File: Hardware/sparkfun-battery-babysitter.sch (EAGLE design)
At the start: 56 parts, among them U1 BQ24075, U2 BQ27441-G1

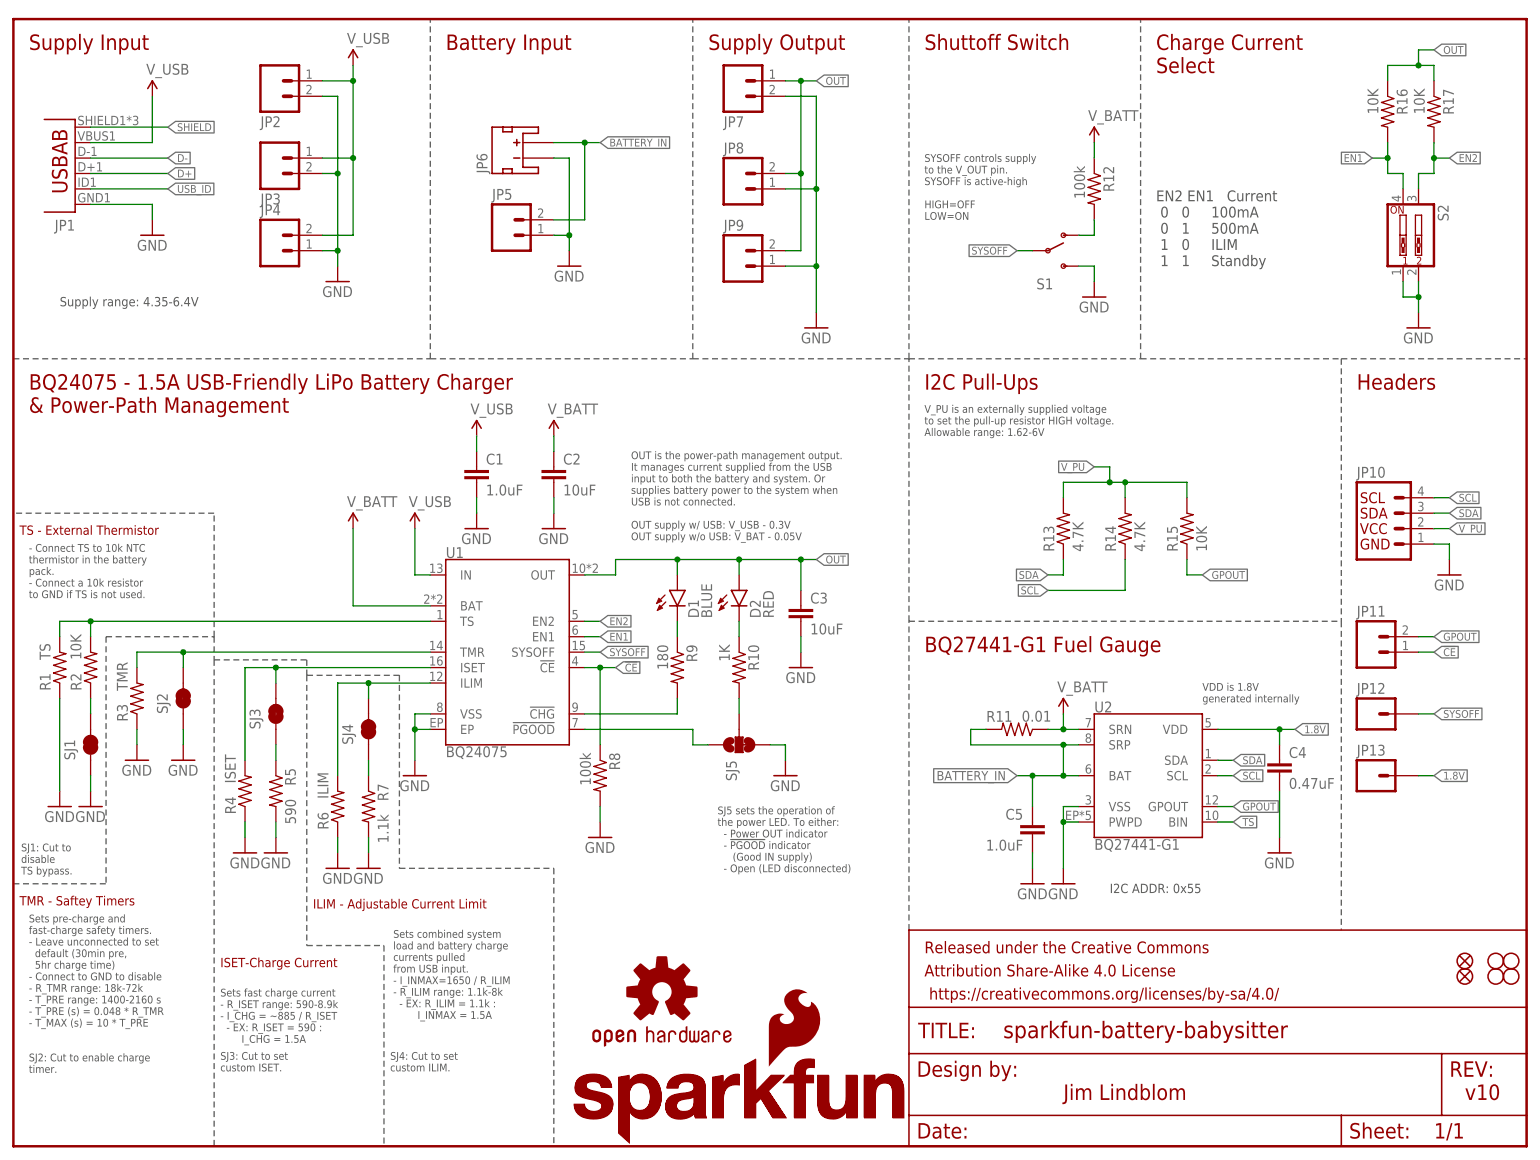
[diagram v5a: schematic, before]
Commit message: Break out D+/D-, silkscreen fixes
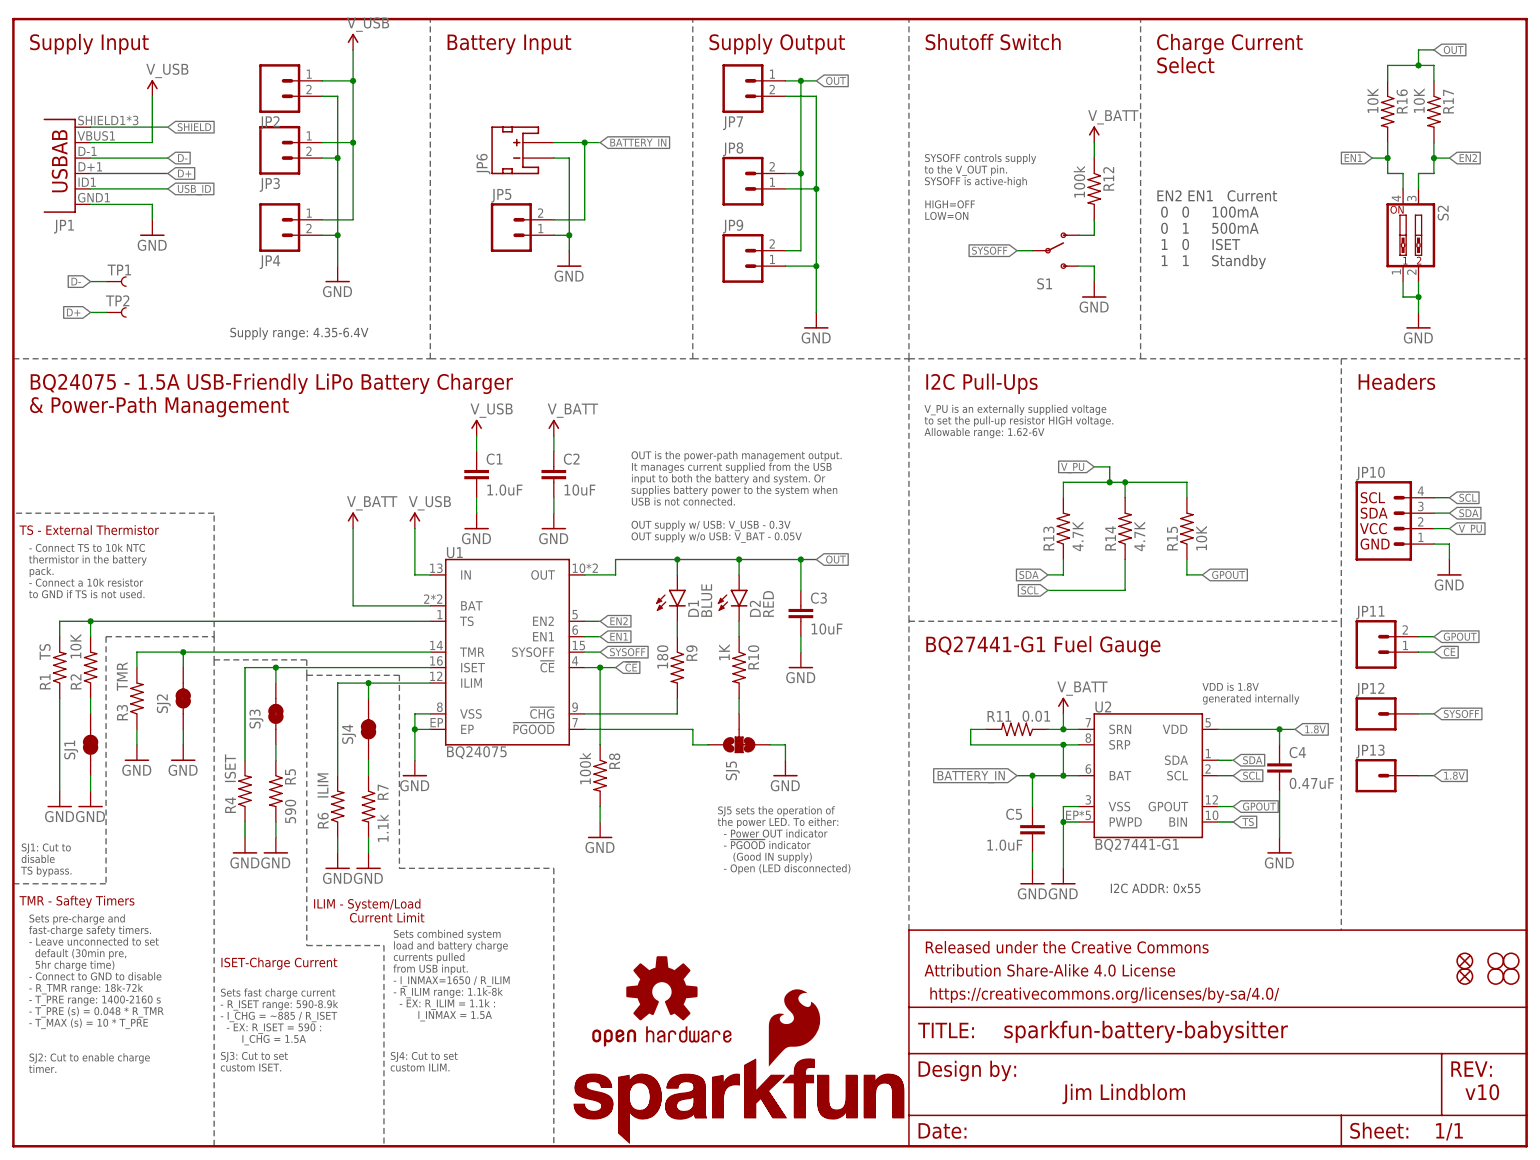
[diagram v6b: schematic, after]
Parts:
- added TP1, TP2: TEST-POINT3X4, SparkFun-Passives:TEST-POINT3X4
- JP4: device SparkFun-Connectors:M02-JST-2-PTH-NO_SILK -> SparkFun-Connectors:M021X02_NO_SILK
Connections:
- net D+: now also TP2.1
- net D-: now also TP1.1
- net GND: now also JP4.2; no longer JP4.1
- net V_USB: now also JP4.1; no longer JP4.2
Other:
- note added: "EN2 EN1 Current 0 0 100mA 0 1 500mA 1 0 ISET 1 1 Standby"
- note added: "ILIM - System/Load Current Limit"
- note added: "Shutoff Switch"
- note removed: "EN2 EN1 Current 0 0 100mA 0 1 500mA 1 0 ILIM 1 1 Standby"
- note removed: "ILIM - Adjustable Current Limit"
- note removed: "Shuttoff Switch"
- moved on the sheet: JP3, JP4
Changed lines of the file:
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@@
 <part name="R16" library="SparkFun-Resistors" deviceset="10KOHM-1/10W-1%(0603)" device="0603" value="10K"/>
 <part name="R17" library="SparkFun-Resistors" deviceset="10KOHM-1/10W-1%(0603)" device="0603" value="10K"/>
-<part name="JP2" library="SparkFun-Connectors" deviceset="M02" device="1X02_NO_SILK"/>
 <part name="R6" library="SparkFun-Resistors" deviceset="RESISTOR" device="PTH-1/6W" value="ILIM"/>
 <part name="GND8" library="SparkFun-Aesthetics" deviceset="GND" device=""/>
@@
 <part name="SJ4" library="SparkFun-Passives" deviceset="JUMPER-PAD-2-NC_BY_TRACE" device="" value=""/>
 <part name="SJ3" library="SparkFun-Passives" deviceset="JUMPER-PAD-2-NC_BY_TRACE" device="" value=""/>
-<part name="JP4" library="SparkFun-Connectors" deviceset="M02" device="-JST-2-PTH-NO_SILK"/>
+<part name="JP4" library="SparkFun-Connectors" deviceset="M02" device="1X02_NO_SILK"/>
 <part name="LOGO1" library="SparkFun-Aesthetics" deviceset="SFE_LOGO_NAME" device=".1_INCH"/>
 <part name="LOGO3" library="SparkFun-Aesthetics" deviceset="OSHW-LOGO" device="S" value="OSHW-LOGOS"/>
@@
 <part name="GND24" library="SparkFun-Aesthetics" deviceset="GND" device=""/>
 <part name="SJ5" library="SparkFun-Passives" deviceset="JUMPER-PAD-3-2OF3_NC_BY_TRACE" device="_SMALL" value=""/>
+<part name="JP2" library="SparkFun-Connectors" deviceset="M02" device="1X02_NO_SILK"/>
+<part name="TP1" library="SparkFun-Passives" deviceset="TEST-POINT" device="3X4" value=""/>
+<part name="TP2" library="SparkFun-Passives" deviceset="TEST-POINT" device="3X4" value=""/>
 </parts>
 <sheets>
@@
  0   0     100mA
  0   1     500mA
- 1   0     ILIM
+ 1   0     ISET
  1   1     Standby</text>
 <text x="34.036" y="25.908" size="1.27" layer="97" align="top-left">Sets fast charge current
@@
 <text x="71.12" y="182.88" size="2.54" layer="94" align="top-left">Battery Input</text>
 <text x="114.3" y="182.88" size="2.54" layer="94" align="top-left">Supply Output</text>
-<text x="149.86" y="182.88" size="2.54" layer="94" align="top-left">Shuttoff Switch</text>
+<text x="149.86" y="182.88" size="2.54" layer="94" align="top-left">Shutoff Switch</text>
 <text x="187.96" y="182.88" size="2.54" layer="94" align="top-left">Charge Current
 Select</text>
@@
 <wire x1="15.24" y1="83.82" x2="33.02" y2="83.82" width="0.2032" layer="97" style="shortdash"/>
 <wire x1="33.02" y1="83.82" x2="33.02" y2="80.01" width="0.2032" layer="97" style="shortdash"/>
-<text x="49.276" y="40.64" size="1.524" layer="94" align="top-left">ILIM - Adjustable Current Limit</text>
+<text x="49.276" y="40.64" size="1.524" layer="94" align="top-left">ILIM - System/Load
+          Current Limit</text>
 <text x="34.036" y="30.988" size="1.524" layer="94" align="top-left">ISET-Charge Current</text>
 <text x="1.016" y="41.148" size="1.524" layer="94" align="top-left">TMR - Saftey Timers</text>
@@
 to set the pull-up resistor HIGH voltage.
 Allowable range: 1.62-6V</text>
-<text x="7.62" y="139.7" size="1.524" layer="97" align="top-left">Supply range: 4.35-6.4V</text>
+<text x="35.56" y="134.62" size="1.524" layer="97" align="top-left">Supply range: 4.35-6.4V</text>
 <text x="195.58" y="76.2" size="1.27" layer="97" align="top-left">VDD is 1.8V
 generated internally</text>
@@
 <instance part="R16" gate="G$1" x="226.06" y="170.18" rot="R270"/>
 <instance part="R17" gate="G$1" x="233.68" y="170.18" rot="R270"/>
-<instance part="JP2" gate="G$1" x="43.18" y="175.26" rot="MR180"/>
 <instance part="R6" gate="G$1" x="53.34" y="55.88" smashed="yes" rot="R90">
 <attribute name="NAME" x="51.8414" y="52.07" size="1.778" layer="95" rot="R90"/>
@@
 <instance part="GND11" gate="1" x="76.2" y="101.6"/>
 <instance part="C1" gate="G$1" x="76.2" y="109.22"/>
-<instance part="SUPPLY2" gate="G$1" x="55.88" y="177.8"/>
+<instance part="SUPPLY2" gate="G$1" x="55.88" y="180.34"/>
 <instance part="GND7" gate="1" x="53.34" y="142.24"/>
 <instance part="STANDOFF3" gate="G$1" x="246.38" y="30.48"/>
@@
 <instance part="STANDOFF4" gate="G$1" x="246.38" y="27.94"/>
 <instance part="S1" gate="1" x="170.18" y="147.32"/>
-<instance part="JP3" gate="G$1" x="43.18" y="162.56" rot="MR180"/>
+<instance part="JP3" gate="G$1" x="43.18" y="165.1" rot="MR180"/>
 <instance part="JP7" gate="G$1" x="119.38" y="175.26" rot="MR180"/>
 <instance part="JP8" gate="G$1" x="119.38" y="157.48"/>
@@
 <instance part="SJ4" gate="G$1" x="58.42" y="68.58" rot="R90"/>
 <instance part="SJ3" gate="G$1" x="43.18" y="71.12" rot="R90"/>
-<instance part="JP4" gate="G$1" x="43.18" y="147.32"/>
+<instance part="JP4" gate="G$1" x="43.18" y="152.4" rot="MR180"/>
 <instance part="LOGO1" gate="G$1" x="90.17" y="0.508"/>
 <instance part="LOGO3" gate="G$1" x="106.68" y="25.4"/>
@@
 <instance part="GND24" gate="1" x="127" y="60.96"/>
 <instance part="SJ5" gate="G$1" x="119.38" y="66.04" rot="MR270"/>
+<instance part="JP2" gate="G$1" x="43.18" y="175.26" rot="MR180"/>
+<instance part="TP1" gate="G$1" x="15.24" y="142.24" smashed="yes">
+<attribute name="NAME" x="15.494" y="143.256" size="1.778" layer="95"/>
+<attribute name="VALUE" x="12.7" y="139.7" size="1.778" layer="96"/>
+</instance>
+<instance part="TP2" gate="G$1" x="15.24" y="137.16" smashed="yes">
+<attribute name="NAME" x="15.24" y="138.176" size="1.778" layer="95"/>
+<attribute name="VALUE" x="12.7" y="134.62" size="1.778" layer="96"/>
+</instance>
 </instances>
 <busses>
@@
 <segment>
 <pinref part="GND7" gate="1" pin="GND"/>
-<wire x1="53.34" y1="172.72" x2="53.34" y2="160.02" width="0.1524" layer="91"/>
+<wire x1="53.34" y1="162.56" x2="53.34" y2="149.86" width="0.1524" layer="91"/>
+<pinref part="JP3" gate="G$1" pin="2"/>
+<wire x1="53.34" y1="149.86" x2="53.34" y2="144.78" width="0.1524" layer="91"/>
+<wire x1="50.8" y1="162.56" x2="53.34" y2="162.56" width="0.1524" layer="91"/>
+<pinref part="JP4" gate="G$1" pin="2"/>
+<wire x1="50.8" y1="149.86" x2="53.34" y2="149.86" width="0.1524" layer="91"/>
+<junction x="53.34" y="149.86"/>
 <pinref part="JP2" gate="G$1" pin="2"/>
-<wire x1="53.34" y1="160.02" x2="53.34" y2="147.32" width="0.1524" layer="91"/>
-<wire x1="53.34" y1="147.32" x2="53.34" y2="144.78" width="0.1524" layer="91"/>
 <wire x1="50.8" y1="172.72" x2="53.34" y2="172.72" width="0.1524" layer="91"/>
-<pinref part="JP3" gate="G$1" pin="2"/>
-<wire x1="50.8" y1="160.02" x2="53.34" y2="160.02" width="0.1524" layer="91"/>
-<junction x="53.34" y="160.02"/>
-<pinref part="JP4" gate="G$1" pin="1"/>
-<wire x1="50.8" y1="147.32" x2="53.34" y2="147.32" width="0.1524" layer="91"/>
-<junction x="53.34" y="147.32"/>
+<wire x1="53.34" y1="172.72" x2="53.34" y2="162.56" width="0.1524" layer="91"/>
+<junction x="53.34" y="162.56"/>
 </segment>
 <segment>
@@
 <label x="25.4" y="160.02" size="1.27" layer="95" xref="yes"/>
 </segment>
+<segment>
+<pinref part="TP2" gate="G$1" pin="1"/>
+<wire x1="15.24" y1="137.16" x2="12.7" y2="137.16" width="0.1524" layer="91"/>
+<label x="12.7" y="137.16" size="1.27" layer="95" rot="R180" xref="yes"/>
+</segment>
 </net>
 <net name="D-" class="0">
@@
 <wire x1="12.7" y1="162.56" x2="25.4" y2="162.56" width="0.1524" layer="91"/>
 <label x="25.4" y="162.56" size="1.27" layer="95" xref="yes"/>
+</segment>
+<segment>
+<pinref part="TP1" gate="G$1" pin="1"/>
+<wire x1="15.24" y1="142.24" x2="12.7" y2="142.24" width="0.1524" layer="91"/>
+<label x="12.7" y="142.24" size="1.27" layer="95" rot="R180" xref="yes"/>
 </segment>
 </net>
@@
 <segment>
 <pinref part="SUPPLY2" gate="G$1" pin="V_USB"/>
-<wire x1="55.88" y1="162.56" x2="55.88" y2="175.26" width="0.1524" layer="91"/>
+<wire x1="55.88" y1="165.1" x2="55.88" y2="175.26" width="0.1524" layer="91"/>
 <pinref part="JP3" gate="G$1" pin="1"/>
-<wire x1="55.88" y1="175.26" x2="55.88" y2="177.8" width="0.1524" layer="91"/>
-<wire x1="50.8" y1="162.56" x2="55.88" y2="162.56" width="0.1524" layer="91"/>
+<wire x1="55.88" y1="175.26" x2="55.88" y2="180.34" width="0.1524" layer="91"/>
+<wire x1="50.8" y1="165.1" x2="55.88" y2="165.1" width="0.1524" layer="91"/>
+<wire x1="55.88" y1="152.4" x2="55.88" y2="165.1" width="0.1524" layer="91"/>
+<junction x="55.88" y="165.1"/>
+<pinref part="JP4" gate="G$1" pin="1"/>
+<wire x1="50.8" y1="152.4" x2="55.88" y2="152.4" width="0.1524" layer="91"/>
 <pinref part="JP2" gate="G$1" pin="1"/>
 <wire x1="50.8" y1="175.26" x2="55.88" y2="175.26" width="0.1524" layer="91"/>
 <junction x="55.88" y="175.26"/>
-<pinref part="JP4" gate="G$1" pin="2"/>
-<wire x1="50.8" y1="149.86" x2="55.88" y2="149.86" width="0.1524" layer="91"/>
-<wire x1="55.88" y1="149.86" x2="55.88" y2="162.56" width="0.1524" layer="91"/>
-<junction x="55.88" y="162.56"/>
 </segment>
 </net>

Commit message: Small silk fixes after run through checklist
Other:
- note added: "Battery Range: 3.3-4.2V"
